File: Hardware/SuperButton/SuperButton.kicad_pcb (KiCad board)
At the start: 2 copper layers, 17 parts, among them J101 USBC, J103 ICSP, SW101 SW_SPST, U102 ATtiny85-20S

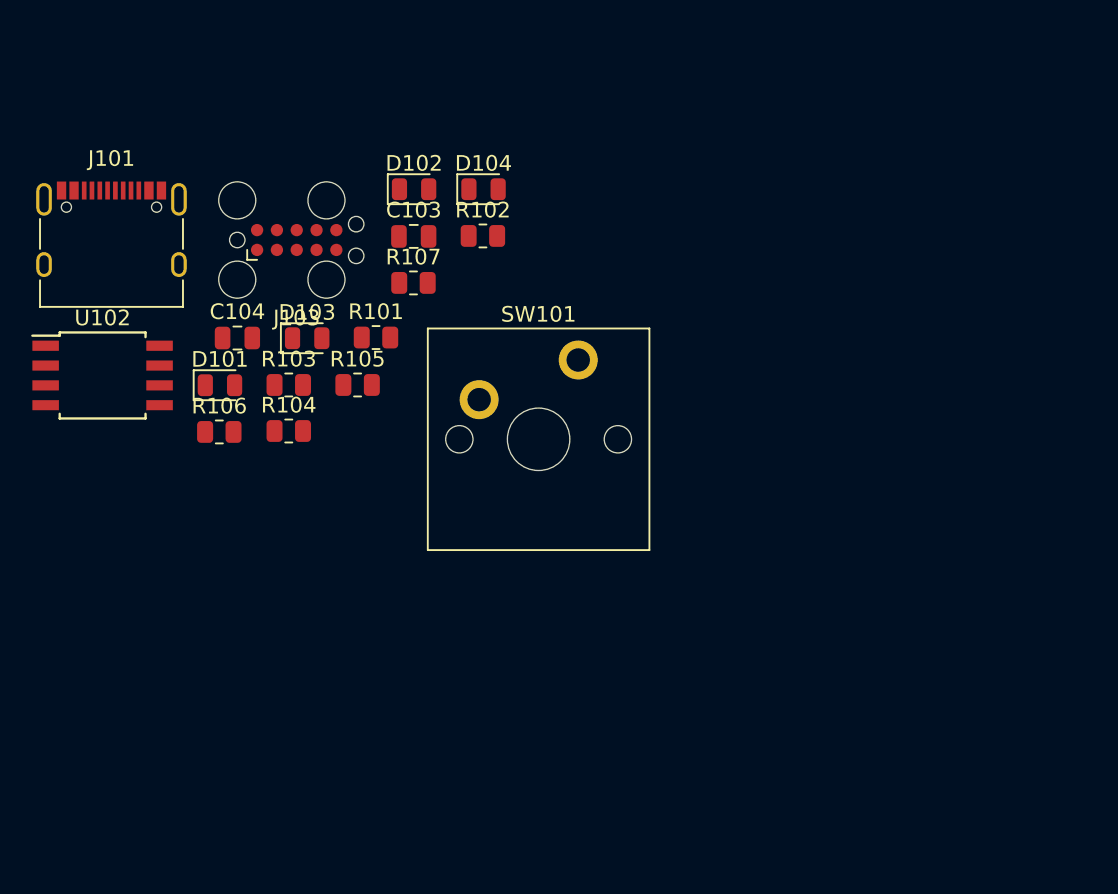
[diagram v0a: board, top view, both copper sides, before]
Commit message: Add board outline
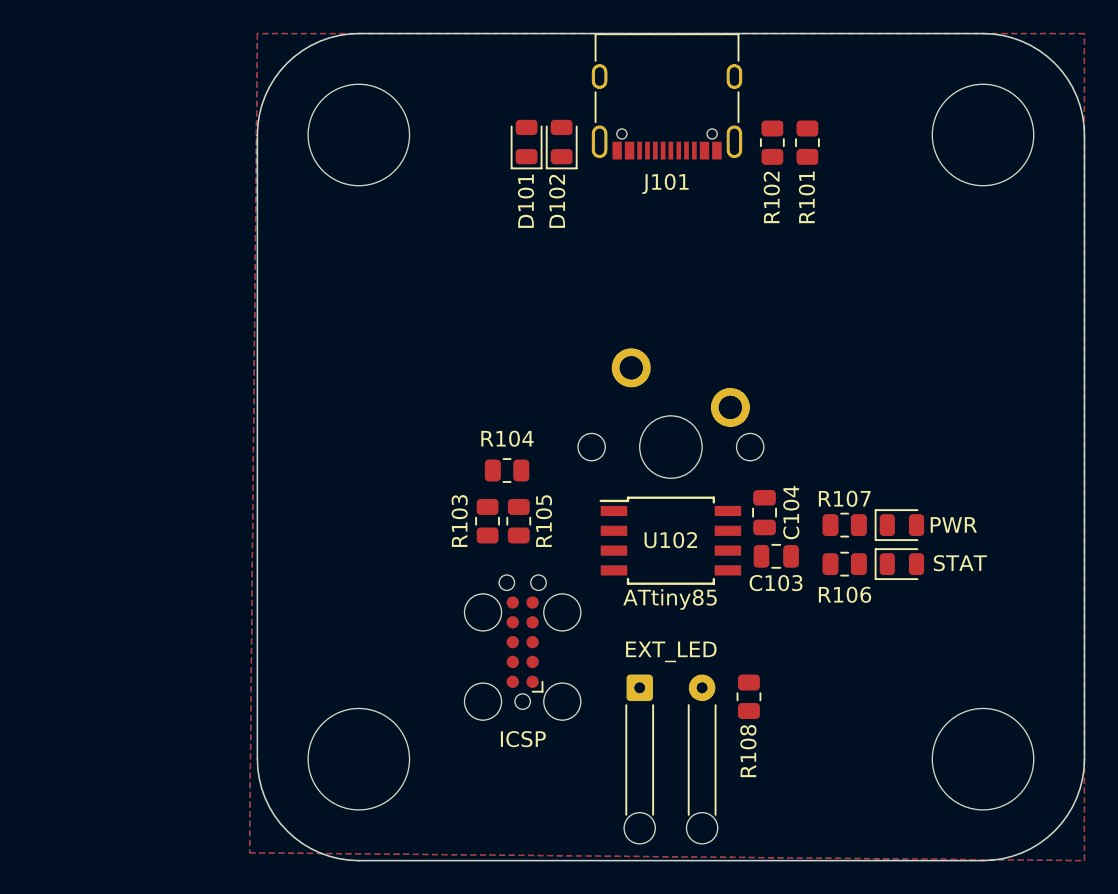
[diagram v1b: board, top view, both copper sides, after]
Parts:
- added G***: LOGO, Misc:QRCODE, B.Cu at (182.0, 109.0)
- added G***: LOGO, 1721:TIDAL_FORCE_LOGO, B.Cu at (190.0, 84.2)
- added H101: MountingHole, MountingHole:MountingHole_6.5mm, B.Cu at (192.0, 110.0)
- added H102: MountingHole, MountingHole:MountingHole_6.5mm, B.Cu at (152.0, 110.0)
- added H103: MountingHole, MountingHole:MountingHole_6.5mm, B.Cu at (152.0, 70.0)
- added H104: MountingHole, MountingHole:MountingHole_6.5mm, B.Cu at (192.0, 70.0)
- added J102: EXT_LED, Connector_Wire:SolderWire-0.15sqmm_1x02_P4mm_D0.5mm_OD1.5mm_Relief, F.Cu at (170.0, 105.4)
- added R108: 1K, Resistor_SMD:R_0805_2012Metric, F.Cu at (177.0, 106.0)
- added REF**: OSHW-Symbol_13.4x12mm_SilkScreen, Symbol:OSHW-Symbol_13.4x12mm_SilkScreen, B.Cu at (153.5, 83.2)
- D103: value SDI -> STAT
- SW101: value SW_SPST -> Switch; moved to B.Cu
- U102: value ATtiny85-20S -> ATtiny85
- moved R106 41.0 mm to (183.1, 97.5)
- moved D103 40.8 mm to (186.8, 97.5)
- moved U102 37.9 mm to (172.0, 96.0)
- moved J101 36.9 mm to (171.7, 67.3), turned to 180 degrees
- moved C104 35.6 mm to (178.0, 94.2), turned to 90 degrees
- moved D104 34.4 mm to (186.8, 95.0)
- moved R107 31.7 mm to (183.1, 95.0)
- moved C103 31.0 mm to (178.7, 97.0)
- moved R101 30.3 mm to (180.7, 70.5), turned to -90 degrees
- moved J103 29.6 mm to (162.5, 102.5), turned to 90 degrees
- moved D101 25.1 mm to (162.7, 70.5), turned to 90 degrees
- moved R102 19.5 mm to (178.5, 70.5), turned to -90 degrees
- moved R103 15.4 mm to (160.2, 94.8), turned to -90 degrees
- moved R104 14.2 mm to (161.5, 91.5)
- moved R105 13.5 mm to (162.2, 94.8), turned to -90 degrees
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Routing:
- added copper zone on B.Cu, net GND
- added copper zone on F.Cu, net GND
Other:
- board outline added: 53 x 53 mm
- board text added: "Super Buttton By FRC 1721 Tidal Force https://www.frc1721.org/ ${FULL_REVISION}"

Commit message: Add ci/cd
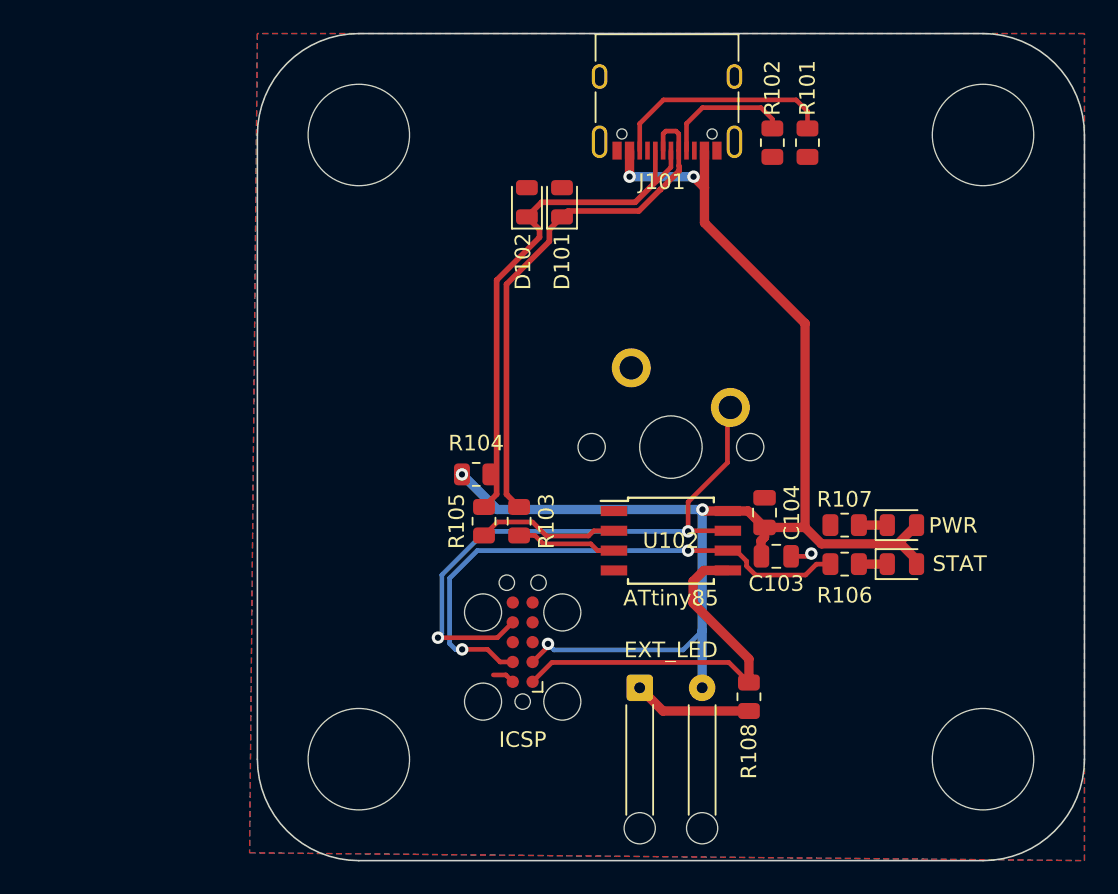
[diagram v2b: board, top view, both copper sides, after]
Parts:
- moved D101 4.48 mm to (165.0, 74.3)
- moved D102 4.45 mm to (162.8, 74.3)
- moved R105 2.23 mm to (160.0, 94.8)
- moved R103 2.02 mm to (162.2, 94.8)
- moved R104 1.99 mm to (159.5, 91.8)
- turned R101 to 90 degrees
- turned R102 to 90 degrees
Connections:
- J101 pad A4: VBUS -> +5V
- J101 pad A9: VBUS -> +5V
- J101 pad B4: VBUS -> +5V
- J101 pad B9: VBUS -> +5V
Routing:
- net +5V: track 0.00 -> 92.5 mm, vias 0 -> 5
- net /SCK: track 0.00 -> 37.9 mm, vias 0 -> 2
- net /SDI: track 0.00 -> 35.0 mm, vias 0 -> 2
- net /USB+: track 0.00 -> 34.0 mm
- net /USB-: track 0.00 -> 33.7 mm
- net /SDO: track 0.00 -> 25.7 mm
- net Net-(J101-PadB5): track 0.00 -> 14.5 mm
- net /USBA: track 0.00 -> 9.20 mm
- net Net-(J101-PadA5): track 0.00 -> 8.55 mm
- net Net-(J102-Pad1): track 0.00 -> 7.62 mm
- net /USBB: track 0.00 -> 6.48 mm
- net GND: track 0.00 -> 2.80 mm, vias 0 -> 1
- net Net-(D104-Pad1): track 0.00 -> 1.82 mm
- net Net-(D103-Pad1): track 0.00 -> 1.82 mm

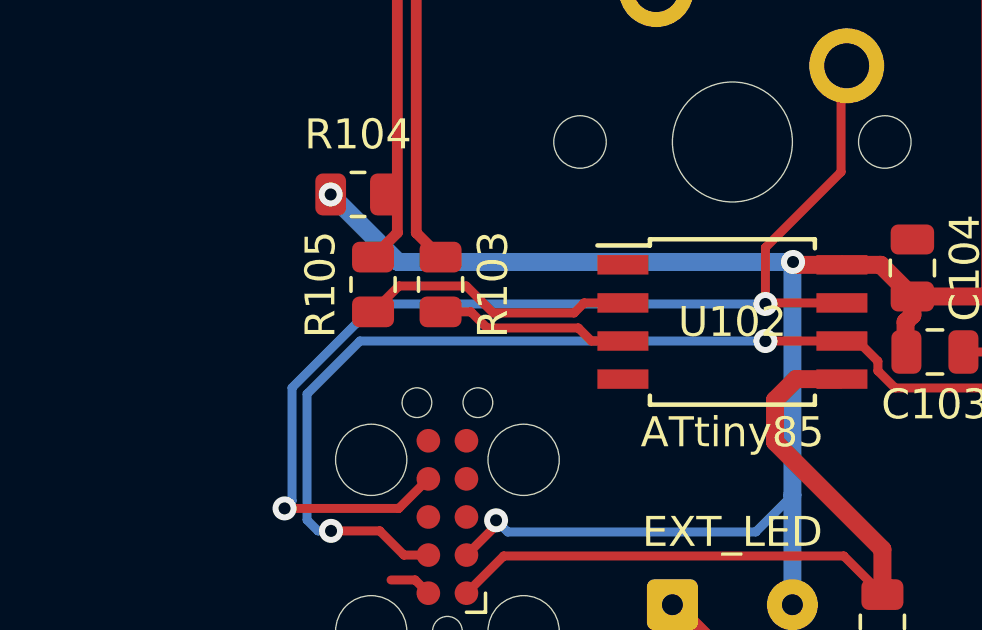
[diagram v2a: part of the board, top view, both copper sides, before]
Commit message: Add reset pullups
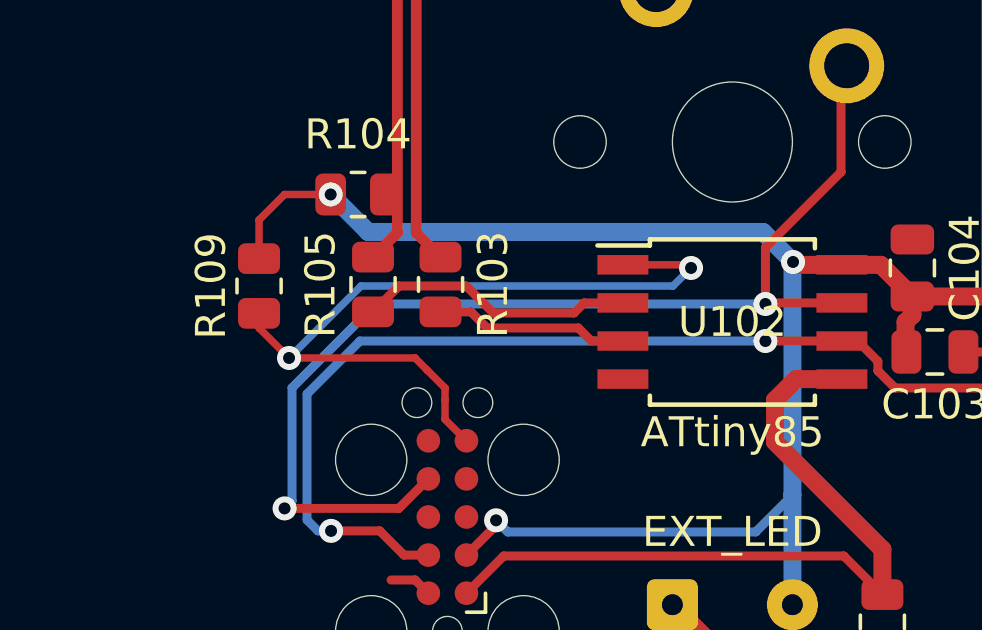
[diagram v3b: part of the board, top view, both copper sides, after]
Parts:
- added R109: 1K, Resistor_SMD:R_0805_2012Metric, F.Cu at (156.2, 94.8)
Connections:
- J103 pad 5: /ICSP_RST -> /RST
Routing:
- net /RST: track 0.00 -> 26.5 mm, vias 0 -> 2
- net +5V: track 92.5 -> 96.5 mm

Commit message: Come back to this later
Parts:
- added U101: ATmega8U2-A, Package_QFP:TQFP-32_7x7mm_P0.8mm, F.Cu at (189.5, 84.2)
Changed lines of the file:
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@@
   (net 20 "/RST")
   (net 21 "Net-(J102-Pad1)")
+  (net 22 "unconnected-(U101-Pad1)")
+  (net 23 "unconnected-(U101-Pad2)")
+  (net 24 "unconnected-(U101-Pad3)")
+  (net 25 "unconnected-(U101-Pad4)")
+  (net 26 "unconnected-(U101-Pad5)")
+  (net 27 "unconnected-(U101-Pad6)")
+  (net 28 "unconnected-(U101-Pad7)")
+  (net 29 "unconnected-(U101-Pad8)")
+  (net 30 "unconnected-(U101-Pad9)")
+  (net 31 "unconnected-(U101-Pad10)")
+  (net 32 "unconnected-(U101-Pad11)")
+  (net 33 "unconnected-(U101-Pad12)")
+  (net 34 "unconnected-(U101-Pad13)")
+  (net 35 "unconnected-(U101-Pad14)")
+  (net 36 "unconnected-(U101-Pad15)")
+  (net 37 "unconnected-(U101-Pad16)")
+  (net 38 "unconnected-(U101-Pad17)")
+  (net 39 "unconnected-(U101-Pad18)")
+  (net 40 "unconnected-(U101-Pad19)")
+  (net 41 "unconnected-(U101-Pad20)")
+  (net 42 "unconnected-(U101-Pad21)")
+  (net 43 "unconnected-(U101-Pad22)")
+  (net 44 "unconnected-(U101-Pad23)")
+  (net 45 "unconnected-(U101-Pad24)")
+  (net 46 "unconnected-(U101-Pad25)")
+  (net 47 "unconnected-(U101-Pad26)")
+  (net 48 "unconnected-(U101-Pad27)")
+  (net 49 "unconnected-(U101-Pad28)")
+  (net 50 "unconnected-(U101-Pad29)")
+  (net 51 "unconnected-(U101-Pad30)")
+  (net 52 "unconnected-(U101-Pad31)")
+  (net 53 "unconnected-(U101-Pad32)")
   (footprint "Diode_SMD:D_0805_2012Metric" (layer "F.Cu")
     (at 162.75 74.3125 90)
@@
       (offset (xyz 0 0 0))
       (scale (xyz 1 1 1))
+      (rotate (xyz 0 0 0))
+    )
+  )
+  (footprint "Package_QFP:TQFP-32_7x7mm_P0.8mm" (layer "F.Cu")
+    (at 189.5 84.25)
+    (descr "32-Lead Plastic Thin Quad Flatpack (PT) - 7x7x1.0 mm Body, 2.00 mm [TQFP] (see Microchip Packaging Specification 00000049BS.pdf)")
+    (tags "QFP 0.8")
+    (property "Sheetfile" "SuperButton.kicad_sch")
+    (property "Sheetname" "")
+    (attr smd)
+    (fp_text reference "U101" (at 0 -6.05) (layer "F.SilkS")
+      (effects (font (size 1 1) (thickness 0.15)))
+    )
+    (fp_text value "ATmega8U2-A" (at 0 6.05) (layer "F.Fab")
+      (effects (font (size 1 1) (thickness 0.15)))
+    )
+    (fp_text user "${REFERENCE}" (at 0 0) (layer "F.Fab")
+      (effects (font (size 1 1) (thickness 0.15)))
+    )
+    (fp_line (start -3.625 -3.625) (end -3.625 -3.4) (layer "F.SilkS") (width 0.15))
+    (fp_line (start -3.625 3.625) (end -3.625 3.3) (layer "F.SilkS") (width 0.15))
+    (fp_line (start 3.625 3.625) (end 3.3 3.625) (layer "F.SilkS") (width 0.15))
+    (fp_line (start -3.625 -3.4) (end -5.05 -3.4) (layer "F.SilkS") (width 0.15))
+    (fp_line (start -3.625 3.625) (end -3.3 3.625) (layer "F.SilkS") (width 0.15))
+    (fp_line (start 3.625 -3.625) (end 3.3 -3.625) (layer "F.SilkS") (width 0.15))
+    (fp_line (start -3.625 -3.625) (end -3.3 -3.625) (layer "F.SilkS") (width 0.15))
+    (fp_line (start 3.625 3.625) (end 3.625 3.3) (layer "F.SilkS") (width 0.15))
+    (fp_line (start 3.625 -3.625) (end 3.625 -3.3) (layer "F.SilkS") (width 0.15))
+    (fp_line (start -5.3 -5.3) (end -5.3 5.3) (layer "F.CrtYd") (width 0.05))
+    (fp_line (start 5.3 -5.3) (end 5.3 5.3) (layer "F.CrtYd") (width 0.05))
+    (fp_line (start -5.3 -5.3) (end 5.3 -5.3) (layer "F.CrtYd") (width 0.05))
+    (fp_line (start -5.3 5.3) (end 5.3 5.3) (layer "F.CrtYd") (width 0.05))
+    (fp_line (start 3.5 3.5) (end -3.5 3.5) (layer "F.Fab") (width 0.15))
+    (fp_line (start 3.5 -3.5) (end 3.5 3.5) (layer "F.Fab") (width 0.15))
+    (fp_line (start -2.5 -3.5) (end 3.5 -3.5) (layer "F.Fab") (width 0.15))
+    (fp_line (start -3.5 3.5) (end -3.5 -2.5) (layer "F.Fab") (width 0.15))
+    (fp_line (start -3.5 -2.5) (end -2.5 -3.5) (layer "F.Fab") (width 0.15))
+    (pad "1" smd rect (at -4.25 -2.8) (size 1.6 0.55) (layers "F.Cu" "F.Paste" "F.Mask")
+      (net 22 "unconnected-(U101-Pad1)") (pinfunction "XTAL1") (pintype "input"))
+    (pad "2" smd rect (at -4.25 -2) (size 1.6 0.55) (layers "F.Cu" "F.Paste" "F.Mask")
+      (net 23 "unconnected-(U101-Pad2)") (pinfunction "PC0/XTAL2") (pintype "bidirectional"))
+    (pad "3" smd rect (at -4.25 -1.2) (size 1.6 0.55) (layers "F.Cu" "F.Paste" "F.Mask")
+      (net 24 "unconnected-(U101-Pad3)") (pinfunction "GND") (pintype "power_in"))
+    (pad "4" smd rect (at -4.25 -0.4) (size 1.6 0.55) (layers "F.Cu" "F.Paste" "F.Mask")
+      (net 25 "unconnected-(U101-Pad4)") (pinfunction "VCC") (pintype "power_in"))
+    (pad "5" smd rect (at -4.25 0.4) (size 1.6 0.55) (layers "F.Cu" "F.Paste" "F.Mask")
+      (net 26 "unconnected-(U101-Pad5)") (pinfunction "PC2") (pintype "bidirectional"))
+    (pad "6" smd rect (at -4.25 1.2) (size 1.6 0.55) (layers "F.Cu" "F.Paste" "F.Mask")
+      (net 27 "unconnected-(U101-Pad6)") (pinfunction "PD0") (pintype "bidirectional"))
+    (pad "7" smd rect (at -4.25 2) (size 1.6 0.55) (layers "F.Cu" "F.Paste" "F.Mask")
+      (net 28 "unconnected-(U101-Pad7)") (pinfunction "PD1") (pintype "bidirectional"))
+    (pad "8" smd rect (at -4.25 2.8) (size 1.6 0.55) (layers "F.Cu" "F.Paste" "F.Mask")
+      (net 29 "unconnected-(U101-Pad8)") (pinfunction "PD2") (pintype "bidirectional"))
+    (pad "9" smd rect (at -2.8 4.25 90) (size 1.6 0.55) (layers "F.Cu" "F.Paste" "F.Mask")
+      (net 30 "unconnected-(U101-Pad9)") (pinfunction "PD3") (pintype "bidirectional"))
+    (pad "10" smd rect (at -2 4.25 90) (size 1.6 0.55) (layers "F.Cu" "F.Paste" "F.Mask")
+      (net 31 "unconnected-(U101-Pad10)") (pinfunction "PD4") (pintype "bidirectional"))
+    (pad "11" smd rect (at -1.2 4.25 90) (size 1.6 0.55) (layers "F.Cu" "F.Paste" "F.Mask")
+      (net 32 "unconnected-(U101-Pad11)") (pinfunction "PD5") (pintype "bidirectional"))
+    (pad "12" smd rect (at -0.4 4.25 90) (size 1.6 0.55) (layers "F.Cu" "F.Paste" "F.Mask")
+      (net 33 "unconnected-(U101-Pad12)") (pinfunction "PD6") (pintype "bidirectional"))
+    (pad "13" smd rect (at 0.4 4.25 90) (size 1.6 0.55) (layers "F.Cu" "F.Paste" "F.Mask")
+      (net 34 "unconnected-(U101-Pad13)") (pinfunction "~{HWB}/PD7") (pintype "bidirectional"))
+    (pad "14" smd rect (at 1.2 4.25 90) (size 1.6 0.55) (layers "F.Cu" "F.Paste" "F.Mask")
+      (net 35 "unconnected-(U101-Pad14)") (pinfunction "PB0") (pintype "bidirectional"))
+    (pad "15" smd rect (at 2 4.25 90) (size 1.6 0.55) (layers "F.Cu" "F.Paste" "F.Mask")
+      (net 36 "unconnected-(U101-Pad15)") (pinfunction "PB1") (pintype "bidirectional"))
+    (pad "16" smd rect (at 2.8 4.25 90) (size 1.6 0.55) (layers "F.Cu" "F.Paste" "F.Mask")
+      (net 37 "unconnected-(U101-Pad16)") (pinfunction "PB2") (pintype "bidirectional"))
+    (pad "17" smd rect (at 4.25 2.8) (size 1.6 0.55) (layers "F.Cu" "F.Paste" "F.Mask")
+      (net 38 "unconnected-(U101-Pad17)") (pinfunction "PB3") (pintype "bidirectional"))
+    (pad "18" smd rect (at 4.25 2) (size 1.6 0.55) (layers "F.Cu" "F.Paste" "F.Mask")
+      (net 39 "unconnected-(U101-Pad18)") (pinfunction "PB4") (pintype "bidirectional"))
+    (pad "19" smd rect (at 4.25 1.2) (size 1.6 0.55) (layers "F.Cu" "F.Paste" "F.Mask")
+      (net 40 "unconnected-(U101-Pad19)") (pinfunction "PB5") (pintype "bidirectional"))
+    (pad "20" smd rect (at 4.25 0.4) (size 1.6 0.55) (layers "F.Cu" "F.Paste" "F.Mask")
+      (net 41 "unconnected-(U101-Pad20)") (pinfunction "PB6") (pintype "bidirectional"))
+    (pad "21" smd rect (at 4.25 -0.4) (size 1.6 0.55) (layers "F.Cu" "F.Paste" "F.Mask")
+      (net 42 "unconnected-(U101-Pad21)") (pinfunction "PB7") (pintype "bidirectional"))
+    (pad "22" smd rect (at 4.25 -1.2) (size 1.6 0.55) (layers "F.Cu" "F.Paste" "F.Mask")
+      (net 43 "unconnected-(U101-Pad22)") (pinfunction "PC7") (pintype "bidirectional"))
+    (pad "23" smd rect (at 4.25 -2) (size 1.6 0.55) (layers "F.Cu" "F.Paste" "F.Mask")
+      (net 44 "unconnected-(U101-Pad23)") (pinfunction "PC6") (pintype "bidirectional"))
+    (pad "24" smd rect (at 4.25 -2.8) (size 1.6 0.55) (layers "F.Cu" "F.Paste" "F.Mask")
+      (net 45 "unconnected-(U101-Pad24)") (pinfunction "PC1/~{RESET}") (pintype "bidirectional"))
+    (pad "25" smd rect (at 2.8 -4.25 90) (size 1.6 0.55) (layers "F.Cu" "F.Paste" "F.Mask")
+      (net 46 "unconnected-(U101-Pad25)") (pinfunction "PC5") (pintype "bidirectional"))
+    (pad "26" smd rect (at 2 -4.25 90) (size 1.6 0.55) (layers "F.Cu" "F.Paste" "F.Mask")
+      (net 47 "unconnected-(U101-Pad26)") (pinfunction "PC4") (pintype "bidirectional"))
+    (pad "27" smd rect (at 1.2 -4.25 90) (size 1.6 0.55) (layers "F.Cu" "F.Paste" "F.Mask")
+      (net 48 "unconnected-(U101-Pad27)") (pinfunction "UCAP") (pintype "passive"))
+    (pad "28" smd rect (at 0.4 -4.25 90) (size 1.6 0.55) (layers "F.Cu" "F.Paste" "F.Mask")
+      (net 49 "unconnected-(U101-Pad28)") (pinfunction "UGND") (pintype "power_in"))
+    (pad "29" smd rect (at -0.4 -4.25 90) (size 1.6 0.55) (layers "F.Cu" "F.Paste" "F.Mask")
+      (net 50 "unconnected-(U101-Pad29)") (pinfunction "D+") (pintype "bidirectional"))
+    (pad "30" smd rect (at -1.2 -4.25 90) (size 1.6 0.55) (layers "F.Cu" "F.Paste" "F.Mask")
+      (net 51 "unconnected-(U101-Pad30)") (pinfunction "D-") (pintype "bidirectional"))
+    (pad "31" smd rect (at -2 -4.25 90) (size 1.6 0.55) (layers "F.Cu" "F.Paste" "F.Mask")
+      (net 52 "unconnected-(U101-Pad31)") (pinfunction "UVCC") (pintype "power_in"))
+    (pad "32" smd rect (at -2.8 -4.25 90) (size 1.6 0.55) (layers "F.Cu" "F.Paste" "F.Mask")
+      (net 53 "unconnected-(U101-Pad32)") (pinfunction "AVCC") (pintype "power_in"))
+    (model "${KICAD6_3DMODEL_DIR}/Package_QFP.3dshapes/TQFP-32_7x7mm_P0.8mm.wrl"
+      (offset (xyz 0 0 0))
+      (scale (xyz 1 1 1))
